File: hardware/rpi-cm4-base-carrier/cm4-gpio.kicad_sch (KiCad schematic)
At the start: 15 parts, among them J1 DNP, J2 USB4105-GF-A, J3 SM04B-SRSS-TB(LF)(SN), U1 74LVC1G07SE-7

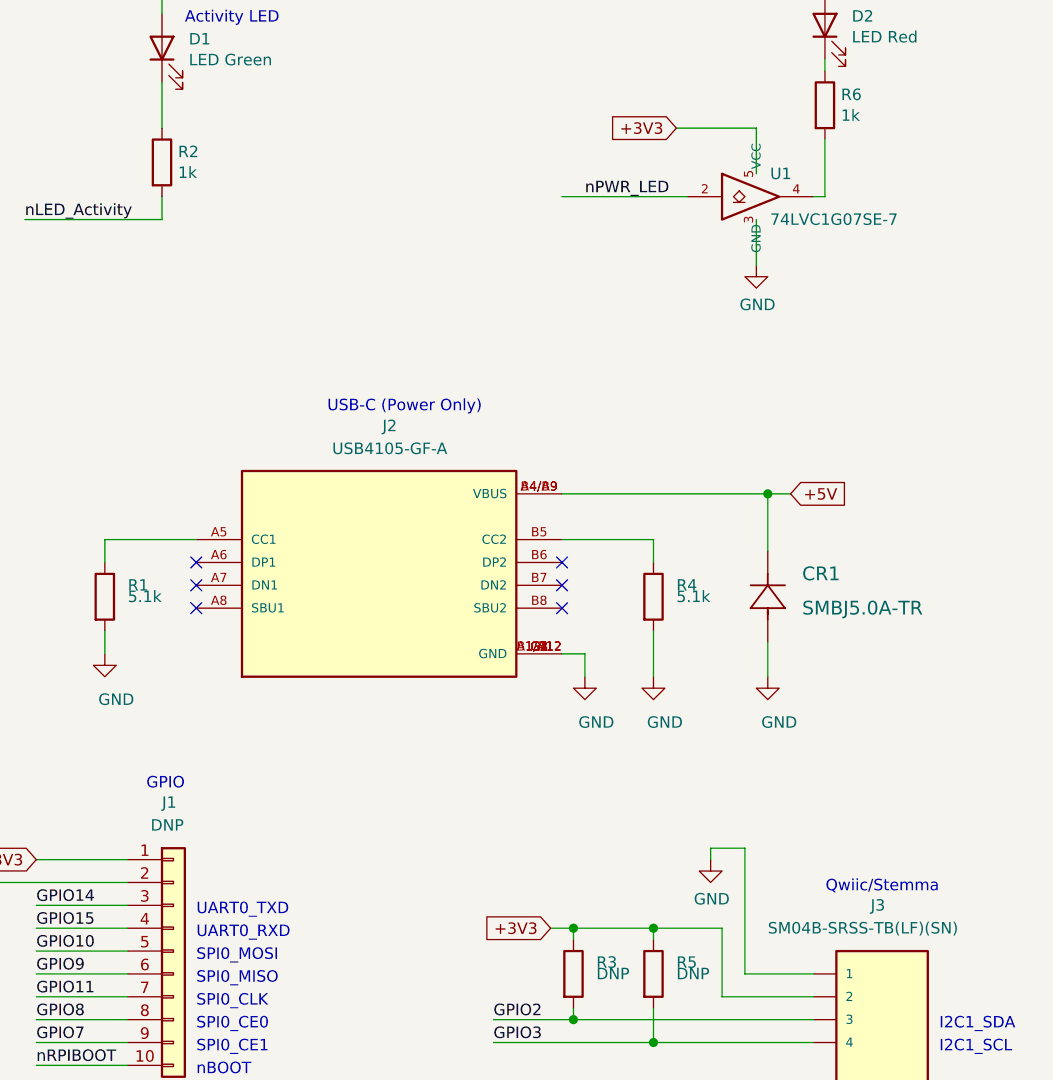
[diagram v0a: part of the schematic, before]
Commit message: routing for some modules progressing quickly, USBHUB mostly complete, thought needed regarding which connectors should be exposed post assembly and which should be for internal use only. LED identifiers and buttons still missing
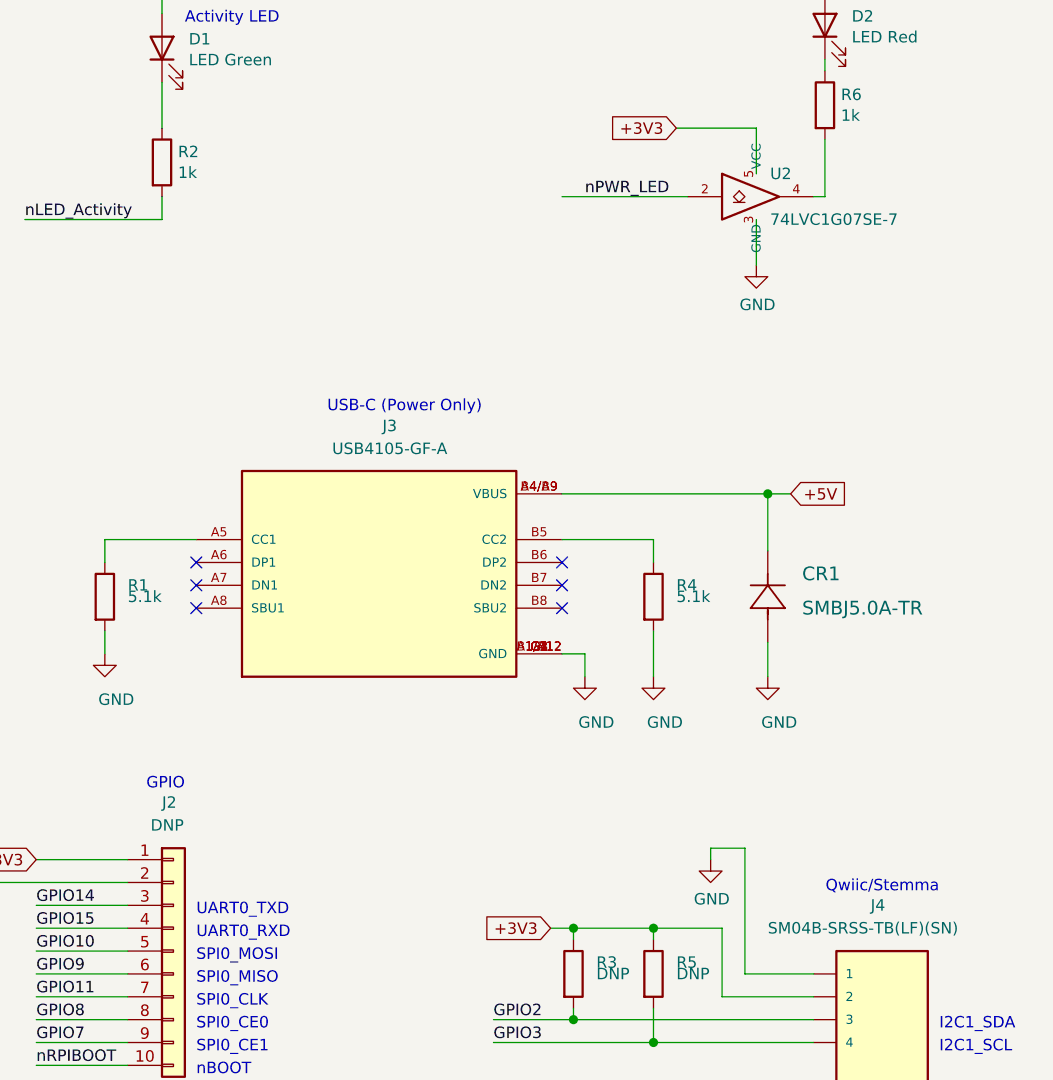
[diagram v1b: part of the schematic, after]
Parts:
- renumbered J1 to J2, J2 to J3, J3 to J4, U1 to U2
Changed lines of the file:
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@@
   (symbol (lib_id "power:GND") (at 152.4 139.7 0) (unit 1)
     (in_bom yes) (on_board yes) (dnp no)
-    (property "Reference" "#PWR0103" (at 152.4 146.05 0)
+    (property "Reference" "#PWR07" (at 152.4 146.05 0)
       (effects (font (size 1.27 1.27)) hide)
     )
@@
       (project "rpi-cm4-base-carrier"
         (path "/92c58705-ecb0-498b-b561-44a3f0daad57/fc4c71a5-1008-4ac4-98db-57c838c57d91"
-          (reference "#PWR0103") (unit 1)
+          (reference "#PWR07") (unit 1)
         )
       )
@@
   (symbol (lib_id "power:GND") (at 233.68 119.38 0) (unit 1)
     (in_bom yes) (on_board yes) (dnp no)
-    (property "Reference" "#PWR0109" (at 233.68 125.73 0)
+    (property "Reference" "#PWR012" (at 233.68 125.73 0)
       (effects (font (size 1.27 1.27)) hide)
     )
@@
       (project "rpi-cm4-base-carrier"
         (path "/92c58705-ecb0-498b-b561-44a3f0daad57/fc4c71a5-1008-4ac4-98db-57c838c57d91"
-          (reference "#PWR0109") (unit 1)
+          (reference "#PWR012") (unit 1)
         )
       )
@@
   (symbol (lib_id "USB4105-GF-A:USB4105-GF-A") (at 196.85 88.9 0) (unit 1)
     (in_bom yes) (on_board yes) (dnp no)
-    (property "Reference" "J2" (at 198.0224 71.1864 0)
+    (property "Reference" "J3" (at 198.0224 71.1864 0)
       (effects (font (size 1.27 1.27)))
     )
@@
       (project "rpi-cm4-base-carrier"
         (path "/92c58705-ecb0-498b-b561-44a3f0daad57/fc4c71a5-1008-4ac4-98db-57c838c57d91"
-          (reference "J2") (unit 1)
+          (reference "J3") (unit 1)
         )
       )
@@
   (symbol (lib_id "power:GND") (at 40.64 175.26 0) (unit 1)
     (in_bom yes) (on_board yes) (dnp no)
-    (property "Reference" "#PWR0101" (at 40.64 181.61 0)
+    (property "Reference" "#PWR05" (at 40.64 181.61 0)
       (effects (font (size 1.27 1.27)) hide)
     )
@@
       (project "rpi-cm4-base-carrier"
         (path "/92c58705-ecb0-498b-b561-44a3f0daad57/fc4c71a5-1008-4ac4-98db-57c838c57d91"
-          (reference "#PWR0101") (unit 1)
+          (reference "#PWR05") (unit 1)
         )
       )
@@
   (symbol (lib_id "SM04B-SRSS-TB_LF__SN_:SM04B-SRSS-TB(LF)(SN)") (at 252.73 137.16 0) (unit 1)
     (in_bom yes) (on_board yes) (dnp no)
-    (property "Reference" "J3" (at 251.46 124.46 0)
+    (property "Reference" "J4" (at 251.46 124.46 0)
       (effects (font (size 1.27 1.27)) (justify left))
     )
@@
       (project "rpi-cm4-base-carrier"
         (path "/92c58705-ecb0-498b-b561-44a3f0daad57/fc4c71a5-1008-4ac4-98db-57c838c57d91"
-          (reference "J3") (unit 1)
+          (reference "J4") (unit 1)
         )
       )
@@
   (symbol (lib_id "power:GND") (at 106.68 175.26 0) (unit 1)
     (in_bom yes) (on_board yes) (dnp no)
-    (property "Reference" "#PWR0102" (at 106.68 181.61 0)
+    (property "Reference" "#PWR06" (at 106.68 181.61 0)
       (effects (font (size 1.27 1.27)) hide)
     )
@@
       (project "rpi-cm4-base-carrier"
         (path "/92c58705-ecb0-498b-b561-44a3f0daad57/fc4c71a5-1008-4ac4-98db-57c838c57d91"
-          (reference "#PWR0102") (unit 1)
+          (reference "#PWR06") (unit 1)
         )
       )
@@
   (symbol (lib_id "power:GND") (at 166.37 96.52 0) (unit 1)
     (in_bom yes) (on_board yes) (dnp no)
-    (property "Reference" "#PWR0104" (at 166.37 102.87 0)
+    (property "Reference" "#PWR09" (at 166.37 102.87 0)
       (effects (font (size 1.27 1.27)) hide)
     )
@@
       (project "rpi-cm4-base-carrier"
         (path "/92c58705-ecb0-498b-b561-44a3f0daad57/fc4c71a5-1008-4ac4-98db-57c838c57d91"
-          (reference "#PWR0104") (unit 1)
+          (reference "#PWR09") (unit 1)
         )
       )
@@
   (symbol (lib_id "power:GND") (at 219.71 99.06 0) (unit 1)
     (in_bom yes) (on_board yes) (dnp no)
-    (property "Reference" "#PWR0106" (at 219.71 105.41 0)
+    (property "Reference" "#PWR010" (at 219.71 105.41 0)
       (effects (font (size 1.27 1.27)) hide)
     )
@@
       (project "rpi-cm4-base-carrier"
         (path "/92c58705-ecb0-498b-b561-44a3f0daad57/fc4c71a5-1008-4ac4-98db-57c838c57d91"
-          (reference "#PWR0106") (unit 1)
+          (reference "#PWR010") (unit 1)
         )
       )
@@
   (symbol (lib_id "Connector_Generic:Conn_01x10") (at 173.99 129.54 0) (unit 1)
     (in_bom yes) (on_board yes) (dnp no)
-    (property "Reference" "J1" (at 172.72 113.03 0)
+    (property "Reference" "J2" (at 172.72 113.03 0)
       (effects (font (size 1.27 1.27)) (justify left))
     )
@@
       (project "rpi-cm4-base-carrier"
         (path "/92c58705-ecb0-498b-b561-44a3f0daad57/fc4c71a5-1008-4ac4-98db-57c838c57d91"
-          (reference "J1") (unit 1)
+          (reference "J2") (unit 1)
         )
       )
@@
   (symbol (lib_id "power:GND") (at 227.33 99.06 0) (unit 1)
     (in_bom yes) (on_board yes) (dnp no)
-    (property "Reference" "#PWR0107" (at 227.33 105.41 0)
+    (property "Reference" "#PWR011" (at 227.33 105.41 0)
       (effects (font (size 1.27 1.27)) hide)
     )
@@
       (project "rpi-cm4-base-carrier"
         (path "/92c58705-ecb0-498b-b561-44a3f0daad57/fc4c71a5-1008-4ac4-98db-57c838c57d91"
-          (reference "#PWR0107") (unit 1)
+          (reference "#PWR011") (unit 1)
         )
       )
@@
   (symbol (lib_id "CM4IO:74LVC1G07_copy") (at 238.76 45.72 0) (unit 1)
     (in_bom yes) (on_board yes) (dnp no)
-    (property "Reference" "U1" (at 240.284 43.18 0)
+    (property "Reference" "U2" (at 240.284 43.18 0)
       (effects (font (size 1.27 1.27)) (justify left))
     )
@@
       (project "rpi-cm4-base-carrier"
         (path "/92c58705-ecb0-498b-b561-44a3f0daad57/fc4c71a5-1008-4ac4-98db-57c838c57d91"
-          (reference "U1") (unit 1)
+          (reference "U2") (unit 1)
         )
       )
@@
   (symbol (lib_id "power:GND") (at 240.03 99.06 0) (unit 1)
     (in_bom yes) (on_board yes) (dnp no)
-    (property "Reference" "#PWR0108" (at 240.03 105.41 0)
+    (property "Reference" "#PWR014" (at 240.03 105.41 0)
       (effects (font (size 1.27 1.27)) hide)
     )
@@
       (project "rpi-cm4-base-carrier"
         (path "/92c58705-ecb0-498b-b561-44a3f0daad57/fc4c71a5-1008-4ac4-98db-57c838c57d91"
-          (reference "#PWR0108") (unit 1)
+          (reference "#PWR014") (unit 1)
         )
       )
@@
   (symbol (lib_id "power:GND") (at 238.76 53.34 0) (unit 1)
     (in_bom yes) (on_board yes) (dnp no)
-    (property "Reference" "#PWR0110" (at 238.76 59.69 0)
+    (property "Reference" "#PWR013" (at 238.76 59.69 0)
       (effects (font (size 1.27 1.27)) hide)
     )
@@
       (project "rpi-cm4-base-carrier"
         (path "/92c58705-ecb0-498b-b561-44a3f0daad57/fc4c71a5-1008-4ac4-98db-57c838c57d91"
-          (reference "#PWR0110") (unit 1)
+          (reference "#PWR013") (unit 1)
         )
       )
@@
   (symbol (lib_id "power:GND") (at 163.83 176.53 0) (unit 1)
     (in_bom yes) (on_board yes) (dnp no)
-    (property "Reference" "#PWR0105" (at 163.83 182.88 0)
+    (property "Reference" "#PWR08" (at 163.83 182.88 0)
       (effects (font (size 1.27 1.27)) hide)
     )
@@
       (project "rpi-cm4-base-carrier"
         (path "/92c58705-ecb0-498b-b561-44a3f0daad57/fc4c71a5-1008-4ac4-98db-57c838c57d91"
-          (reference "#PWR0105") (unit 1)
-        )
-      )
+          (reference "#PWR08") (unit 1)
+        )
+      )

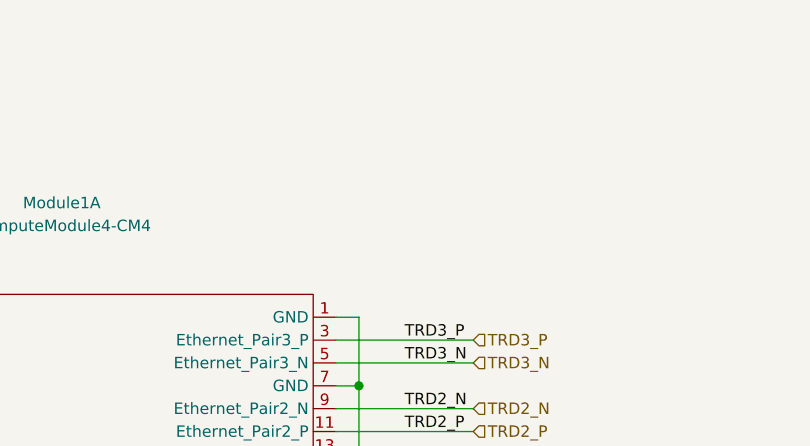
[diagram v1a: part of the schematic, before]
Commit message: addition of 4xRGB LED's and I2C driver, also includes right angle lightpipe
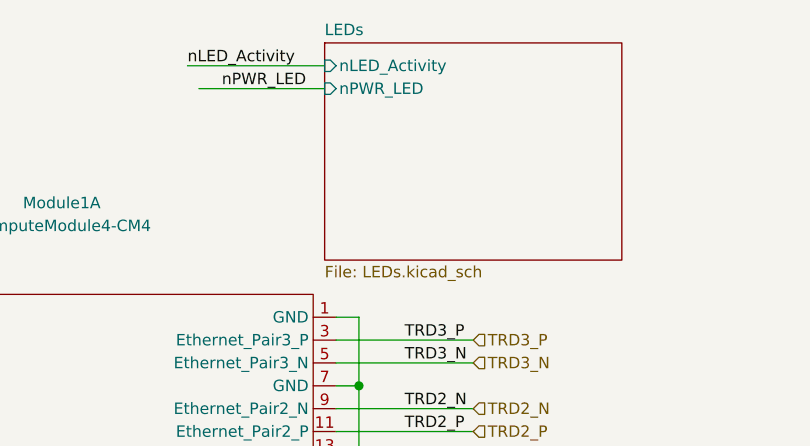
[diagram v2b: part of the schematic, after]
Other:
- added sheet LEDs (LEDs.kicad_sch)
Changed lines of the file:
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@@
+    (stroke (width 0) (type solid))
+  )
+  (wire (pts (xy 87.63 17.78) (xy 102.87 17.78))
     (stroke (width 0) (type solid))
   )
@@
     (stroke (width 0) (type default))
   )
+  (wire (pts (xy 88.9 20.32) (xy 102.87 20.32))
+    (stroke (width 0) (type solid))
+  )
   (wire (pts (xy 40.64 83.82) (xy 40.64 96.52))
     (stroke (width 0) (type solid))
@@
     (effects (font (size 1.27 1.27)) (justify left bottom))
   )
+  (label "nLED_Activity" (at 87.63 17.78 0) (fields_autoplaced)
+    (effects (font (size 1.27 1.27)) (justify left bottom))
+  )
   (label "GPIO8" (at 158.75 137.16 0) (fields_autoplaced)
     (effects (font (size 1.27 1.27)) (justify left bottom))
@@
   )
   (label "EEPROM_nWP" (at 139.7 173.99 0) (fields_autoplaced)
+    (effects (font (size 1.27 1.27)) (justify left bottom))
+  )
+  (label "nPWR_LED" (at 91.44 20.32 0) (fields_autoplaced)
     (effects (font (size 1.27 1.27)) (justify left bottom))
   )
@@
       )
     )
+  )
+  (sheet (at 102.87 15.24) (size 33.02 24.13) (fields_autoplaced)
+    (stroke (width 0.1524) (type solid))
+    (fill (color 0 0 0 0.0000))
+    (property "Sheetname" "LEDs" (at 102.87 14.5284 0)
+      (effects (font (size 1.27 1.27)) (justify left bottom))
+    )
+    (property "Sheetfile" "LEDs.kicad_sch" (at 102.87 39.9546 0)
+      (effects (font (size 1.27 1.27)) (justify left top))
+    )
+    (pin "nLED_Activity" input (at 102.87 17.78 180)
+      (effects (font (size 1.27 1.27)) (justify left))
+    )
+    (pin "nPWR_LED" input (at 102.87 20.32 180)
+      (effects (font (size 1.27 1.27)) (justify left))
+    )
+    (instances
+      (project "rpi-cm4-base-carrier"
+        (path "/92c58705-ecb0-498b-b561-44a3f0daad57/fc4c71a5-1008-4ac4-98db-57c838c57d91" (page "8"))
+      )
+    )

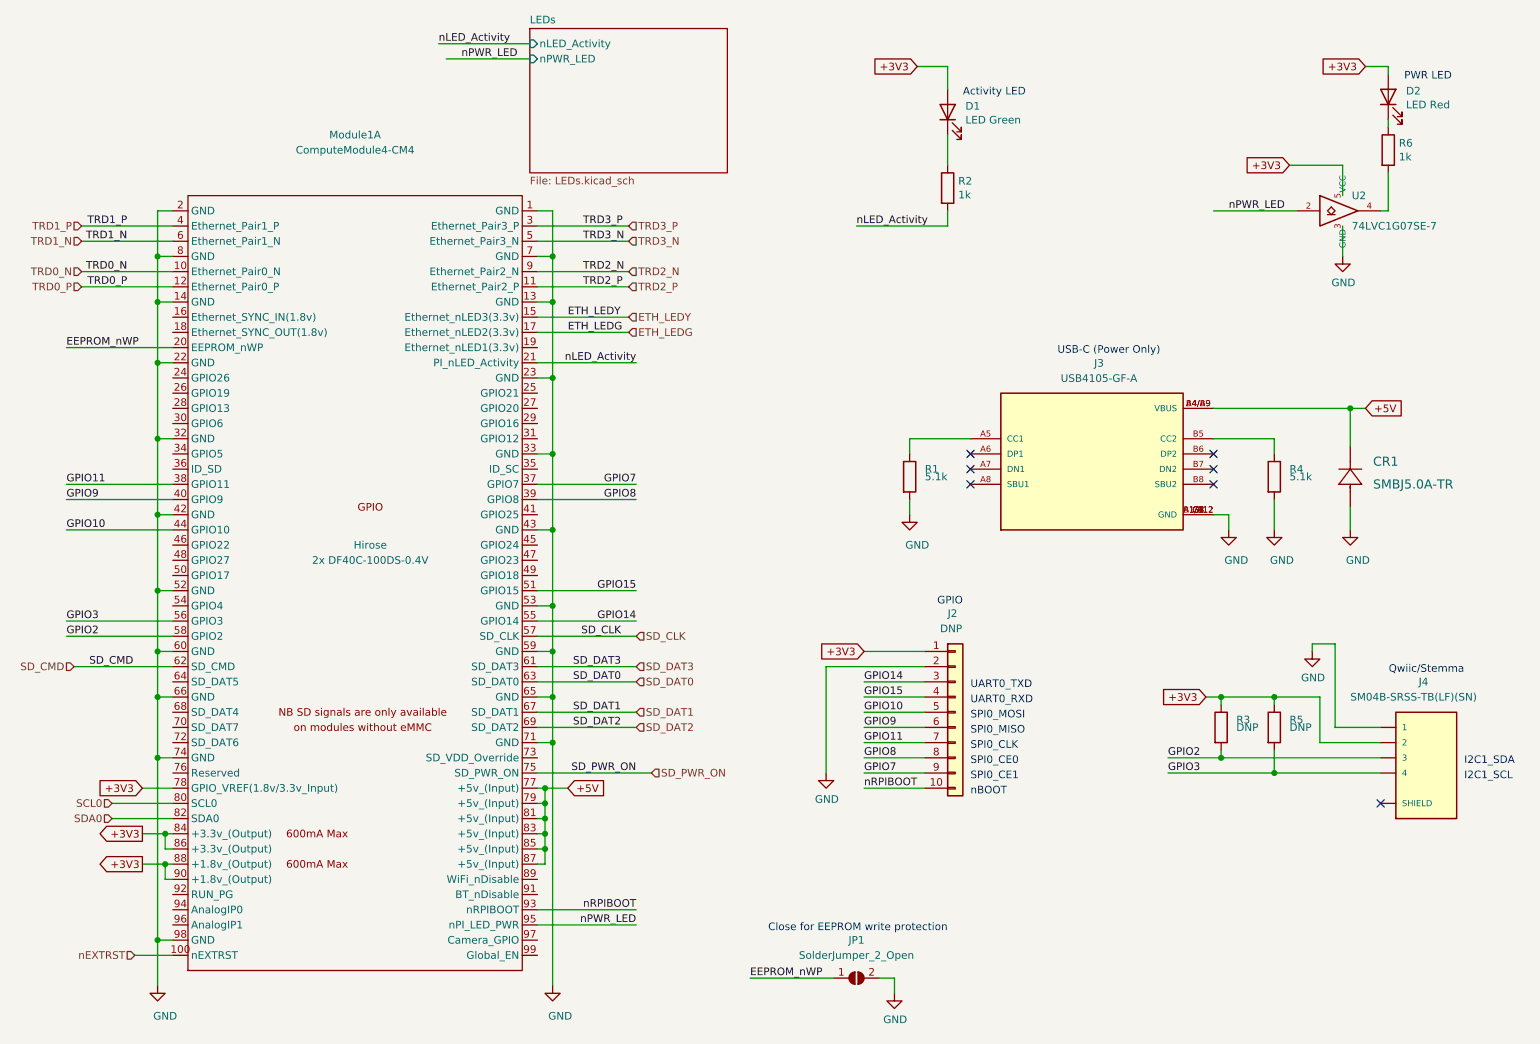
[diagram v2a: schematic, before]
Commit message: started final placement of blocks, realised ESD suppression devices cannot be manufactured with JLC, need to switch part
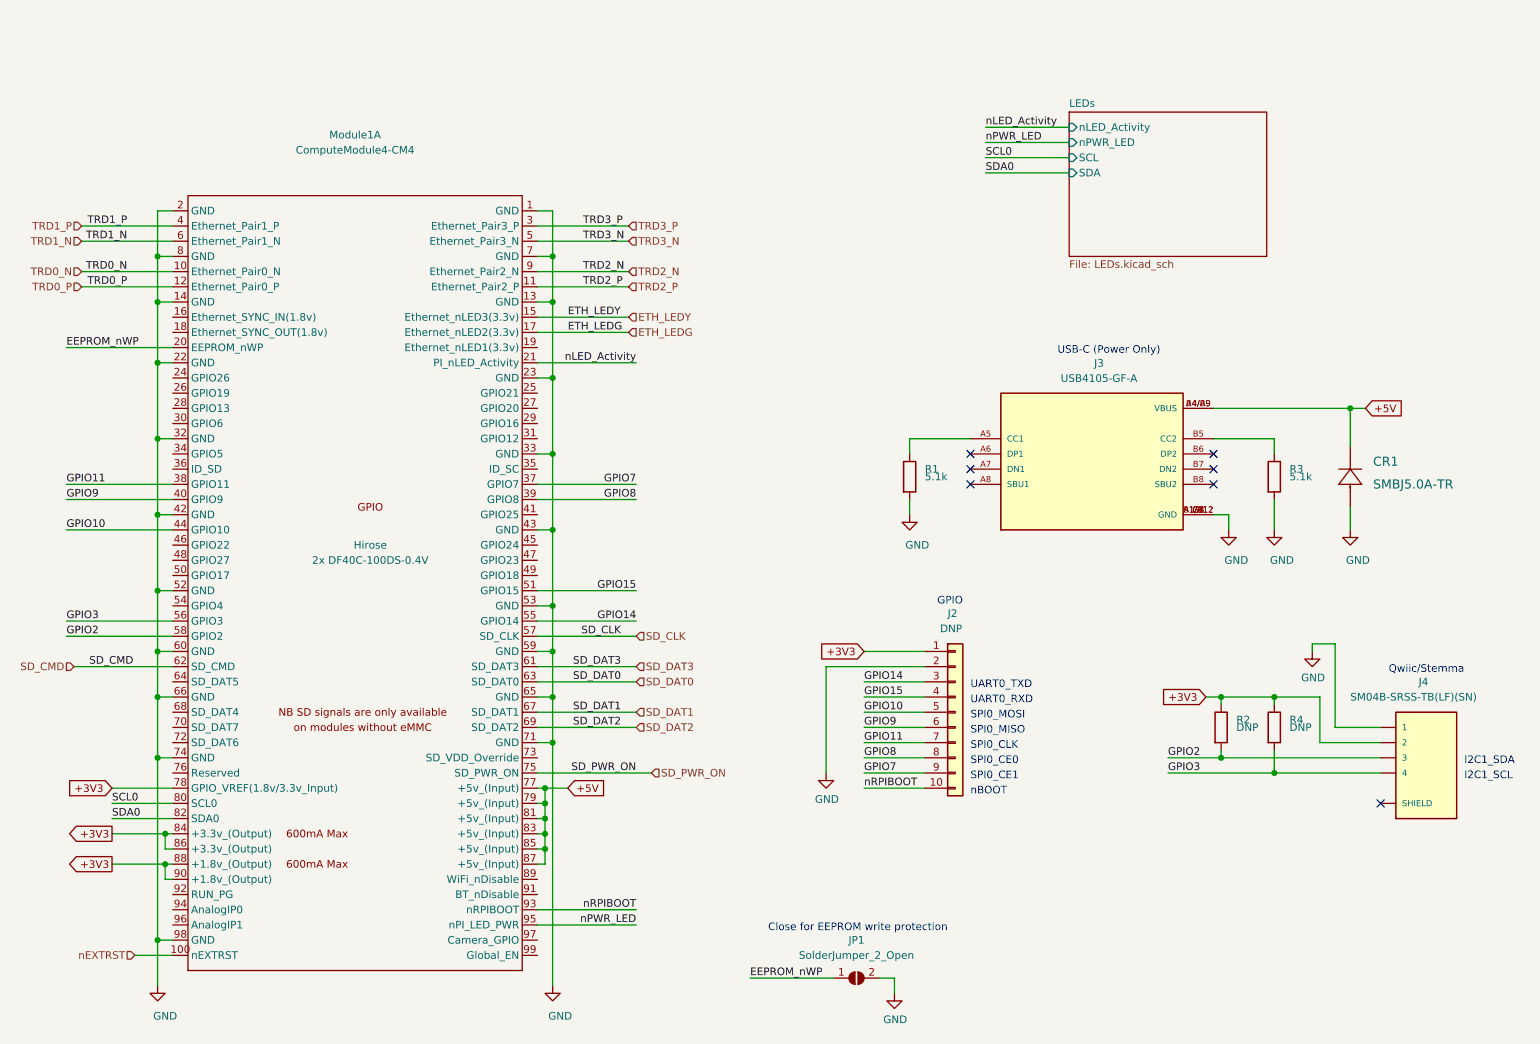
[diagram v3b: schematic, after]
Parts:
- removed D1: LED Green, LED_SMD:LED_0603_1608Metric, symbol Device:LED
- removed D2: LED Red, LED_SMD:LED_0603_1608Metric, symbol Device:LED
- removed R2, R6: 1k, Resistor_SMD:R_0603_1608Metric_Pad0.98x0.95mm_HandSolder, symbol Device:R
- removed U2: 74LVC1G07SE-7, Package_TO_SOT_SMD:SOT-353_SC-70-5, symbol CM4IO:74LVC1G07_copy
- renumbered R3 to R2, R4 to R3, R5 to R4
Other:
- sheet LEDs ports: added SCL, SDA; removed none
- note removed: "Activity LED"
- note removed: "PWR LED"
